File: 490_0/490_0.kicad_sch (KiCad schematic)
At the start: 250 parts, among them J1 ArduCAM ToF Connector, J10 Conn_01x02_Pin, J12 HDMI_D_1.4, J13 DF40C-100DS-0.4V_51_, J14 Micro_SD_Card, J15 USB_B_Micro, J16 Conn_01x02_Pin, J17 Conn_01x03_Pin, J2 ArduCAM ToF Connector, J3 DF40C-100DS-0.4V_51_, J5 Conn_01x02_Pin, J6 Conn_01x02_Pin, J7 Conn_01x02_Pin, J8 USB3_A_Stacked, J9 Conn_01x02_Pin, P1 USB_C_Plug_USB2.0, Q1 NMOS, Q2 NMOS, Q3 NMOS, Q4 NMOS, Q5 NMOS, Q7 NMOS, Q8 FS8205A, SW1 SW_DPST_x2, SW2 SW_Push0, SW3 SW_Push1, SW4 SW_Push2, SW5 SW_Push3, SW6 SW_Push4, SW7 SW_Push, U1 TUSB7320RKMR, U10 ECMF04-4HSWM10, U11 74HC4051, U12 RT9742GGJ5, U13 MAX98357A, U14 MAX98357A, U15 MP2632BGR-Z, U16 TP4057, U17 DW01, U18 TPS61023DRLR, U2 TPS2560DRCR, U3 PCA9685, U4 ECMF04-4HSWM10, U5 ECMF04-4HSWM10, U6 BD9G401EFJ, U9 ECMF04-4HSWM10, X1 ECS-480-18-33-JGN-TR

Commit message: Arranged schematic
Added sheets (as in the phase 2 presentation)
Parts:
- removed C0(ceramic)1, C0(ceramic)2, C0(ceramic)3, C0(ceramic)4, C0(ceramic)5, C5(ceramic)1, C6(ceramic)1, Cx(ceramic)1: 100nF, Capacitor_SMD:C_0603_1608Metric, symbol Device:C
- removed C0(radial)1, C0(radial)2, C0(radial)3, C0(radial)4, C0(radial)5, C5(radial)1, C6(radial)1, Cx(radial)1: 10uF, Capacitor_THT:CP_Radial_D5.0mm_P2.50mm, symbol Device:C
- removed C1, C2, C62: 22u, symbol PCM_Elektuur:C
- removed C10, C11, C13, C14, C15, C16, C18, C19, C20, C21, C23, C25, C26, C28, C3, C30, C31, C33, C37, C38, C39, C40, C41, C42, C43, C46, C5, C52, C53, C6, C7, C9: 100n, symbol PCM_Elektuur:C
- removed C12, C17, C22, C24, C27, C29, C32, C34, C4, C44, C45, C8: 10n, symbol PCM_Elektuur:C
- removed C35, C36: 18p, symbol PCM_Elektuur:C
- removed C47, C63, C67: 0.1u, symbol PCM_Elektuur:C
- removed C48, C49: 150u, Capacitor_THT:CP_Radial_D5.0mm_P2.50mm, symbol PCM_SL_Devices:Capacitor_PO
- removed C50: 47u, symbol PCM_Elektuur:C
- removed C51: 10u, symbol PCM_Elektuur:C
- removed C54: 0.01u, symbol PCM_Elektuur:C
- removed C55: 4.7u, symbol PCM_Elektuur:C
- removed C56, Cin1: 10uF, symbol Device:C
- removed C64, C65, C66, C68: TBD, symbol PCM_Elektuur:C
- removed D1, D11, D12, D2, D3: USBULC6-2M6, PCM_Package_TO_SOT_SMD_AKL:SOT-666, symbol PCM_Diode_TVS_AKL:USBLC6-2P6
- removed D10, D4, D5, D6, D9: D, symbol Device:D
- removed D13, D15, D16, D17, D18, D19: LED, symbol Device:LED
- removed D20: RBR5LAM60A, symbol PCM_Diode_Schottky_AKL:D_Schottky_Generic
- removed D7, D8: LED, PCM_SparkFun-LED:LED_0603_1608Metric, symbol PCM_SparkFun-LED:LED
- removed FB1: 220 @ 100 MHz, symbol Device:FerriteBead
- removed FB2, FB3: FerriteBead, Capacitor_SMD:C_0603_1608Metric, symbol Device:FerriteBead_Small
- removed J1, J2: ArduCAM ToF Connector, symbol Connector_Generic:Conn_02x15_Counter_Clockwise
- removed J10, J5, J6, J7, J9: Conn_01x02_Pin, symbol Connector:Conn_01x02_Pin
- removed J12: HDMI_D_1.4, symbol Connector:HDMI_D_1.4
- removed J13, J3: DF40C-100DS-0.4V_51_, DF40C-100DS-0.4V_51_:HIROSE_DF40C-100DS-0.4V_51_, symbol capstone_parts:DF40C-100DS-0.4V_51_
- removed J14: Micro_SD_Card, symbol Connector:Micro_SD_Card
- removed J17: Conn_01x03_Pin, symbol Connector:Conn_01x03_Pin
- removed J8: USB3_A_Stacked, symbol Connector:USB3_A_Stacked
- removed JP1: SJ_A0, Jumper:SolderJumper-2_P1.3mm_Open_RoundedPad1.0x1.5mm, symbol Jumper:SolderJumper_2_Open
- removed JP10, JP11, JP12: SolderJumper, Jumper:SolderJumper-2_P1.3mm_Open_RoundedPad1.0x1.5mm, symbol Jumper:SolderJumper_2_Open
- removed JP13: SolderJumper_3_Open, symbol Jumper:SolderJumper_3_Open
- removed JP2: SJ_A1, Jumper:SolderJumper-2_P1.3mm_Open_RoundedPad1.0x1.5mm, symbol Jumper:SolderJumper_2_Open
- removed JP3: SJ_A2, Jumper:SolderJumper-2_P1.3mm_Open_RoundedPad1.0x1.5mm, symbol Jumper:SolderJumper_2_Open
- removed JP4: SJ_A3, Jumper:SolderJumper-2_P1.3mm_Open_RoundedPad1.0x1.5mm, symbol Jumper:SolderJumper_2_Open
- removed JP5: SJ_A4, Jumper:SolderJumper-2_P1.3mm_Open_RoundedPad1.0x1.5mm, symbol Jumper:SolderJumper_2_Open
- removed JP6: SJ_A5, Jumper:SolderJumper-2_P1.3mm_Open_RoundedPad1.0x1.5mm, symbol Jumper:SolderJumper_2_Open
- removed JP7, JP8, JP9: SolderJumper, rJumper:SolderJumper-3_P1.3mm_Open_RoundedPad1.0x1.5mm, symbol Jumper:SolderJumper_3_Open
- removed L1, L3: 2.2uH, PCM_SparkFun-Coil:0806, symbol PCM_SparkFun-Coil:2.2uH_0806_1.2A
- removed P1: USB_C_Plug_USB2.0, symbol Connector:USB_C_Plug_USB2.0
- removed PD1, PU1, R36, R40, Rgd1, Rgd2, Rgd3, Rgd4, Rgd5: 100K, symbol Device:R
- removed Q1, Q2, Q3, Q4, Q5, Q7: NMOS, symbol Simulation_SPICE:NMOS
- removed R1: 4.7k, symbol PCM_Elektuur:R
- removed R10, R11, R14, R15: R, symbol PCM_Elektuur:R
- removed R12, R13, R16, R17, R49, R50, R53, R54, R55, R56, R57, R58, R59: TBD, symbol Device:R
- removed R18: 4.7k, symbol Device:R
- removed R1G$1, R1G$2, R1G$3, R1G$4, R1G$5, R1G$6, R7: 10K, symbol Device:R
- removed R2, R3, R6, R8, R9: 10k, symbol PCM_Elektuur:R
- removed R21, R22, R23, R24, R25, R26, R27, R28, R29, R30, R32, R33, R34, R35, R37, R38, R39: R, symbol Device:R
- removed R31: 12K 1%, symbol Device:R
- removed R4: 1M, symbol PCM_Elektuur:R
- removed R48: 5.1k, symbol Device:R
- removed R5: 9.09k 1%, symbol PCM_Elektuur:R
- removed R51: 49.9k, symbol Device:R
- removed R52: 10m, symbol Device:R
- removed Rg1, Rg2, Rg3, Rg4, Rg5: 220, symbol Device:R
- removed S1: Speaker_Left, Connector_JST:JST_PH_S2B-PH-K_1x02_P2.00mm_Horizontal, symbol Connector_Generic:Conn_01x02
- removed S2: Speaker_Right, Connector_JST:JST_PH_S2B-PH-K_1x02_P2.00mm_Horizontal, symbol Connector_Generic:Conn_01x02
- removed SW1: SW_DPST_x2, symbol Switch:SW_DPST_x2
- removed SW2: SW_Push0, symbol Switch:SW_Push
- removed SW3: SW_Push1, symbol Switch:SW_Push
- removed SW4: SW_Push2, symbol Switch:SW_Push
- removed SW5: SW_Push3, symbol Switch:SW_Push
- removed SW6: SW_Push4, symbol Switch:SW_Push
- removed SW7: SW_Push, symbol Switch:SW_Push
- removed U1: TUSB7320RKMR, RKM100_5P5X5P5, symbol capstone_parts:TUSB7320RKMR
- removed U10, U4, U5, U9: ECMF04-4HSWM10, Package_DFN_QFN:UDFN-10_1.35x2.6mm_P0.5mm, symbol Power_Protection:ECMF04-4HSWM10
- removed U11: 74HC4051, symbol 74xx:74HC4051
- removed U12: RT9742GGJ5, TSOT-23-5_RIT, symbol capstone_parts:RT9742GGJ5
- removed U13, U14: MAX98357A, Package_DFN_QFN:TQFN-16-1EP_3x3mm_P0.5mm_EP1.23x1.23mm_ThermalVias, symbol Audio:MAX98357A
- removed U15: MP2632BGR-Z, IC26_MP2632BGR-Z_MNP, symbol capstone_parts:MP2632BGR-Z
- removed U2: TPS2560DRCR, TPS2560DRCR:VREG_V62_16624-01YE, symbol capstone_parts:TPS2560DRCR
- removed U3: PCA9685, PCA9685:TSSOP28, symbol capstone_parts:PCA9685
- removed U6: BD9G401EFJ, symbol capstone_parts:BD9G401EFJ-E2
- removed X1: ECS-480-18-33-JGN-TR, symbol PCM_Elektuur_1:X-crystal
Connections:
- no-connect marks 112 -> 2
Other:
- added sheet Board Connector A (board_connector_a.kicad_sch)
- added sheet Camera CSI Connectors (cameras.kicad_sch)
- added sheet Charging and Power (charging_power.kicad_sch)
- added sheet HDMI (hdmi.kicad_sch)
- added sheet PCI Bridge (pci_bridge.kicad_sch)
- added sheet PWM and Motors (pwm_motors.kicad_sch)
- added sheet Push Button Circuits (pushbuttons.kicad_sch)
- added sheet Speakers (speakers.kicad_sch)
- added sheet microSD Module (micro_sd.kicad_sch)
- note added: "Ferhaan Hawas (40224777) Ardalan Jamshidi (27079265) Gabriel Lemieux (40031680) Arthur Mosnier (40122836) Anass Taoussi (40229052) Frankies Vat (40218933)"
- note added: "Object Recognition and Haptic Guidance Headband for Blind Users"
- note removed: "I2C Address = 1 + A5 + A4 + A3 + A2 + A1 + RW Open = 0 / Closed = 1"
- note removed: "Micro HDMI"
- note removed: "PCIe to USB 3.0 bridge"
- note removed: "PCM_CLK"
- note removed: "PCM_DIN"
- note removed: "PCM_FS"
- note removed: "PWM and Motors"
- note removed: "Push-buttons"
- note removed: "REMOVE, RASPBERRY CAN ALREADY DO THIS"
- note removed: "SD_POWER_ON"
- note removed: "Sample MUX for the PWM substitution"
- note removed: "Speaker (Left)"
- note removed: "Speaker (Right)"
- note removed: "The chip is designed if we dont have PWM"
- note removed: "Vibration Motor #1"
- note removed: "Vibration Motor #2"
- note removed: "Vibration Motor #3"
- note removed: "Vibration Motor #4"
- note removed: "Vibration Motor #5"
- note removed: "^For Charge current"
- moved on the sheet: C57, C58, C59, C60, C61, D14, J15, J16, L2, LED3, LED4, Q8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

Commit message: Minor updates
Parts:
- removed C57: 100n, symbol PCM_Elektuur:C
- removed C58: 10uF, PCM_SparkFun-Capacitor:C_0603_1608Metric, symbol PCM_SparkFun-Capacitor:10uF_0603_10V_20%
- removed C59, C61: ?, symbol PCM_Elektuur:C
- removed C60: 0.1uF, PCM_SparkFun-Capacitor:C_0402_1005Metric, symbol PCM_SparkFun-Capacitor:0.1uF_0402_16V_10%
- removed D14: USBULC6-2M6, PCM_Package_TO_SOT_SMD_AKL:SOT-666, symbol PCM_Diode_TVS_AKL:USBLC6-2P6
- removed J15: USB_B_Micro, symbol Connector:USB_B_Micro
- removed J16: Conn_01x02_Pin, symbol Connector:Conn_01x02_Pin
- removed L2: 1u, WE-MAPI_4030:WE-MAPI_4030, symbol capstone_parts:74438357010
- removed LED3: LED_1.8mm_Red, PCM_LED_THT_AKL:LED_D1.8mm_W3.3mm_H2.4mm, symbol PCM_LED_AKL:LED_1.8mm_Red
- removed LED4: LED_1.8mm_SMD_Green, PCM_LED_SMD_AKL:LED_1.8mm_GullWing, symbol PCM_LED_AKL:LED_1.8mm_SMD_Green
- removed Q8: FS8205A, FS8205A:SOP65P640X120-8N, symbol FS8205A:FS8205A
- removed R41, R42: 1k, Resistor_THT:R_Axial_DIN0207_L6.3mm_D2.5mm_P10.16mm_Horizontal, symbol PCM_SL_Resistors:1k
- removed R43, R44: 2k_0603, 4ms_Resistor:R_0603, symbol PCM_4ms_Resistor:2k_0603
- removed R45: 100ohm, Resistor_THT:R_Axial_DIN0207_L6.3mm_D2.5mm_P10.16mm_Horizontal, symbol PCM_SL_Resistors:100ohm
- removed R46, R47: ?, Resistor_THT:R_Axial_DIN0207_L6.3mm_D2.5mm_P10.16mm_Horizontal, symbol PCM_SL_Resistors:100ohm
- removed U16: TP4057, Package_TO_SOT_SMD:TSOT-23-6, symbol Battery_Management:TP4057
- removed U17: DW01, DW01:SOT23-6, symbol capstone_parts:DW01
- removed U18: TPS61023DRLR, DRL0006A, symbol capstone_parts:TPS61023DRLR
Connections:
- no-connect marks 2 -> 0
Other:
- added sheet USB 2.0 Bridge (untitled.kicad_sch)
- note removed: "Battery Charging and Power Supply Unit"

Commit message: updates
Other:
- removed sheet PCI Bridge
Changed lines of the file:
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@@
-	)
-	(sheet
-		(at 295.91 99.06)
-		(size 43.18 27.94)
-		(exclude_from_sim no)
-		(in_bom yes)
-		(on_board yes)
-		(dnp no)
-		(fields_autoplaced yes)
-		(stroke
-			(width 0.1524)
-			(type solid)
-		)
-		(fill
-			(color 0 0 0 0.0000)
-		)
-		(property "Sheetname" "PCI Bridge"
-			(at 295.91 98.3484 0)
-			(effects
-				(font
-					(size 1.27 1.27)
-				)
-				(justify left bottom)
-			)
-		)
-		(property "Sheetfile" "pci_bridge.kicad_sch"
-			(at 295.91 127.5846 0)
-			(effects
-				(font
-					(size 1.27 1.27)
-				)
-				(justify left top)
-			)
-		)
-		(instances
-			(project "490_0"
-				(path "/365a82ed-827d-43e1-aa2f-b98221c4179c"
-					(page "6")
-				)
-			)
-		)
 	)
 	(sheet

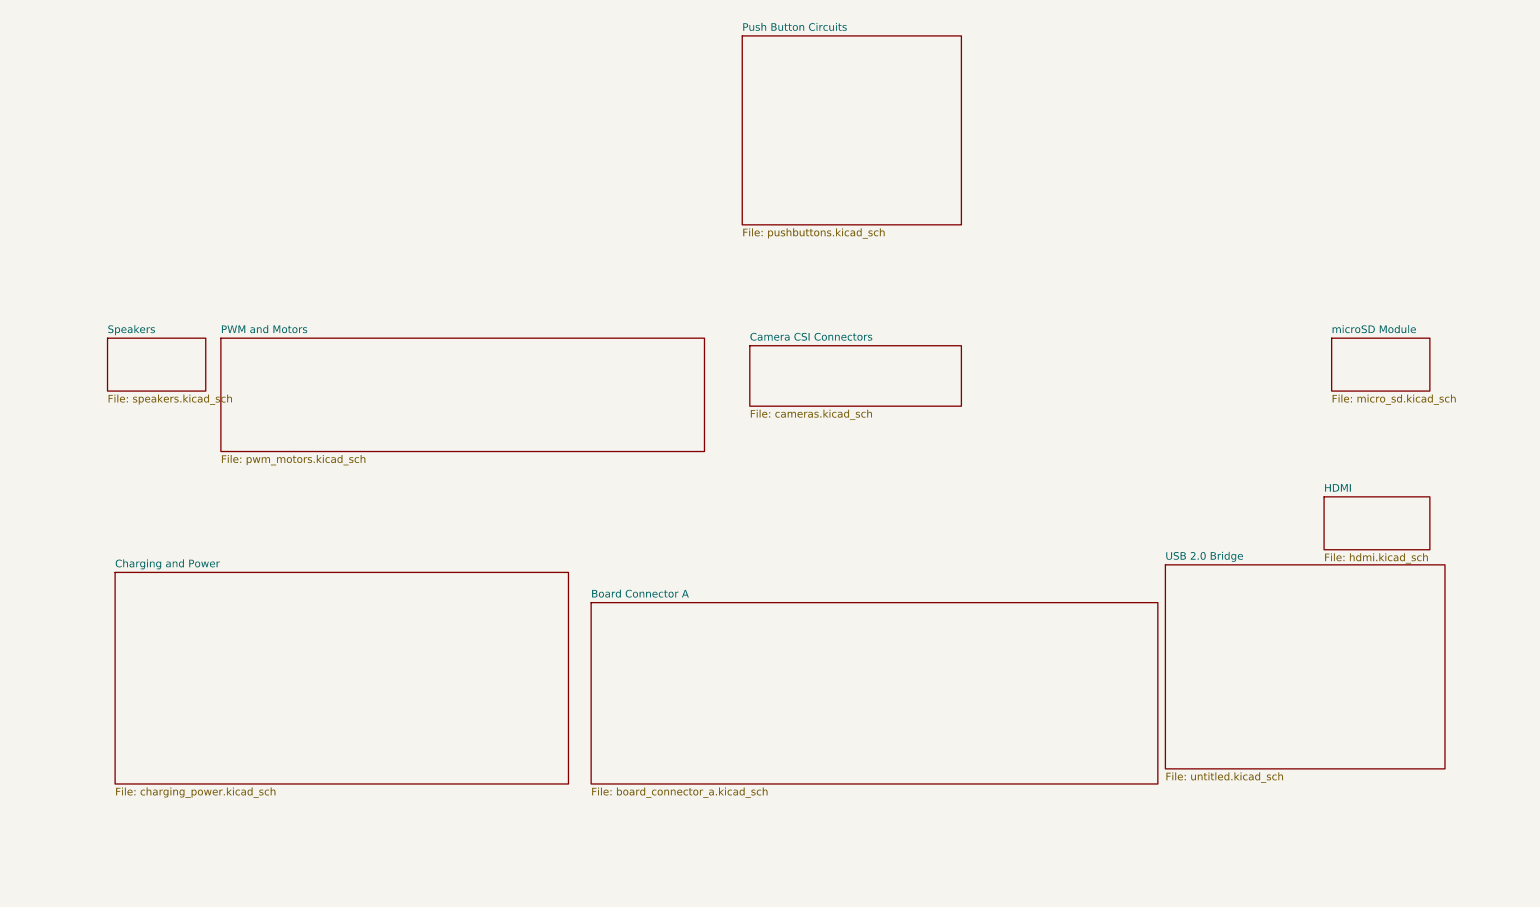
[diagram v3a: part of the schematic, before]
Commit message: Updated box diagram
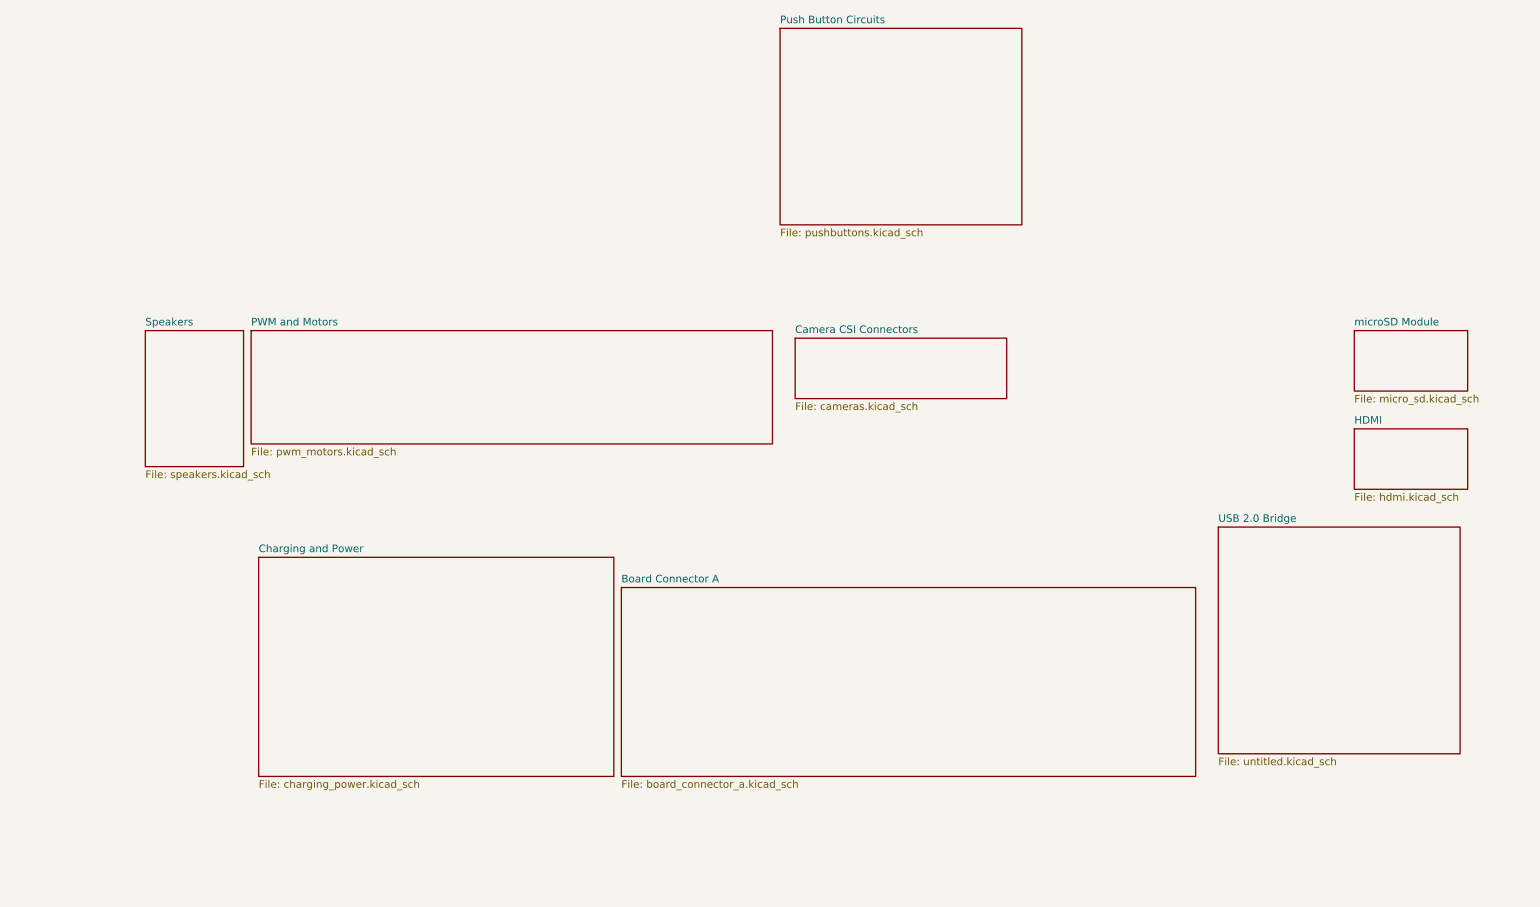
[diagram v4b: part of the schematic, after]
